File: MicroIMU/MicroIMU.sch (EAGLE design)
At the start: 18 parts, among them IC1 LSM303DLHC

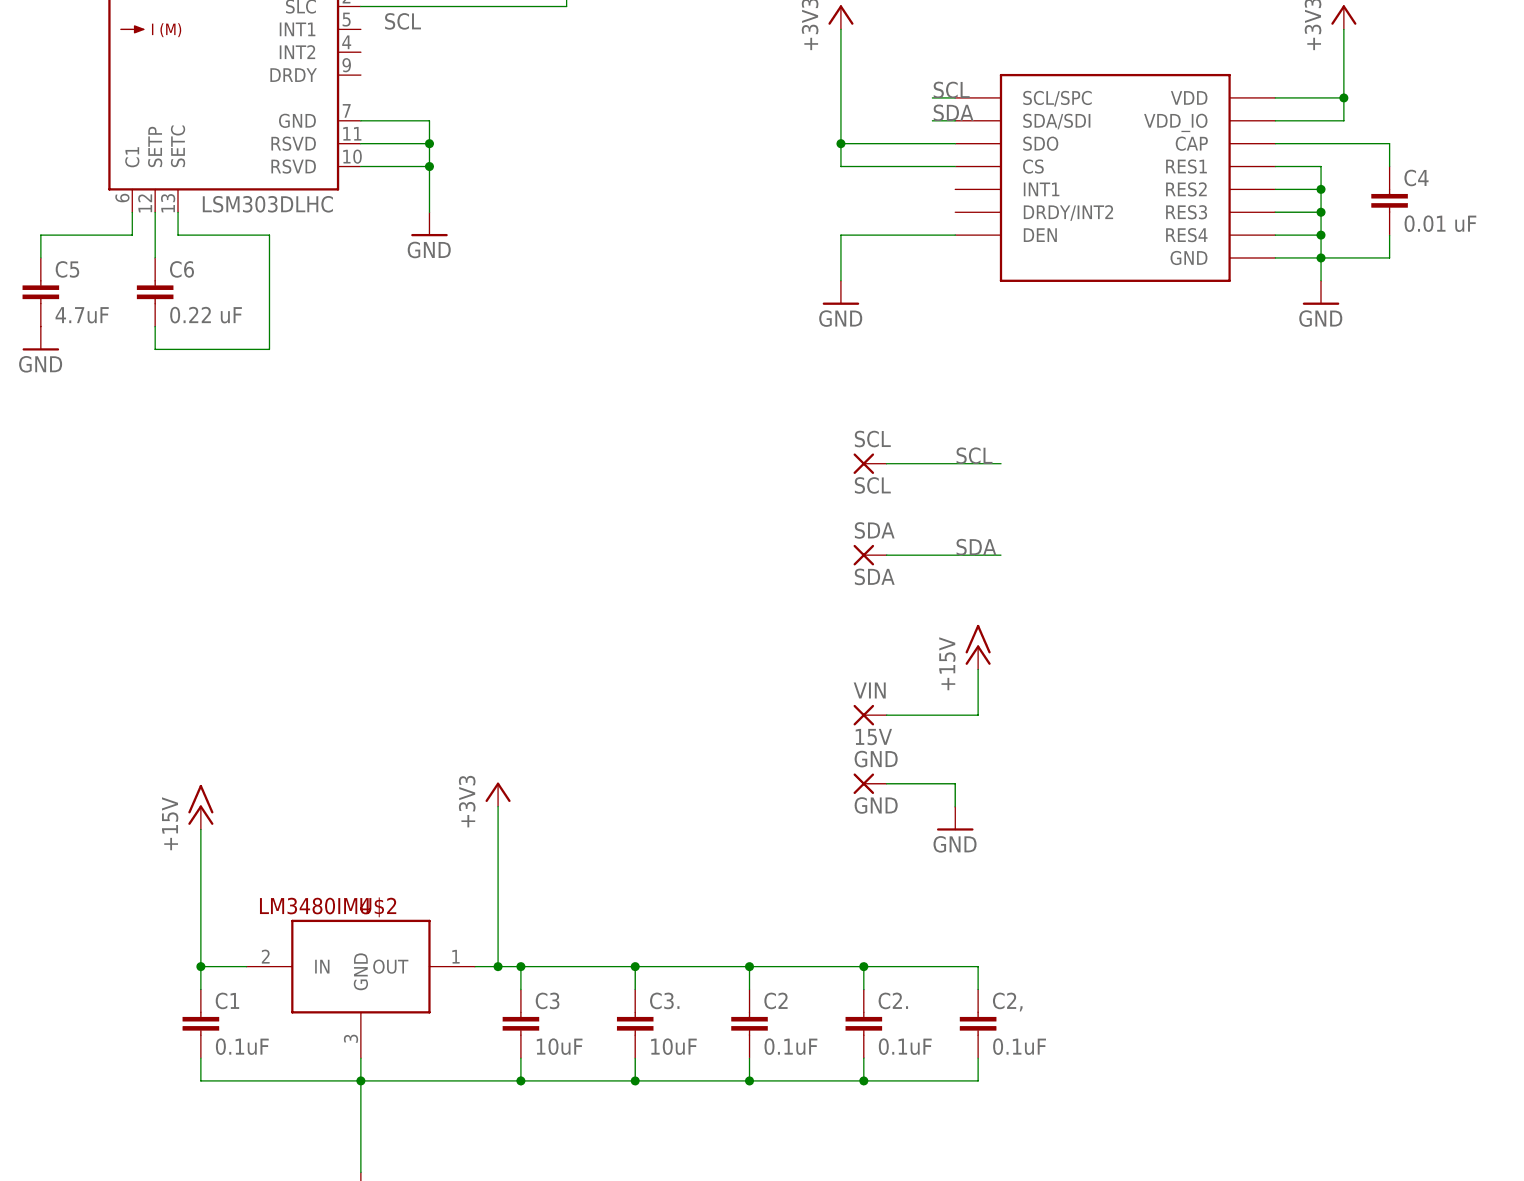
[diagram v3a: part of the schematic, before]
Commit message: Improved silkscreen labels
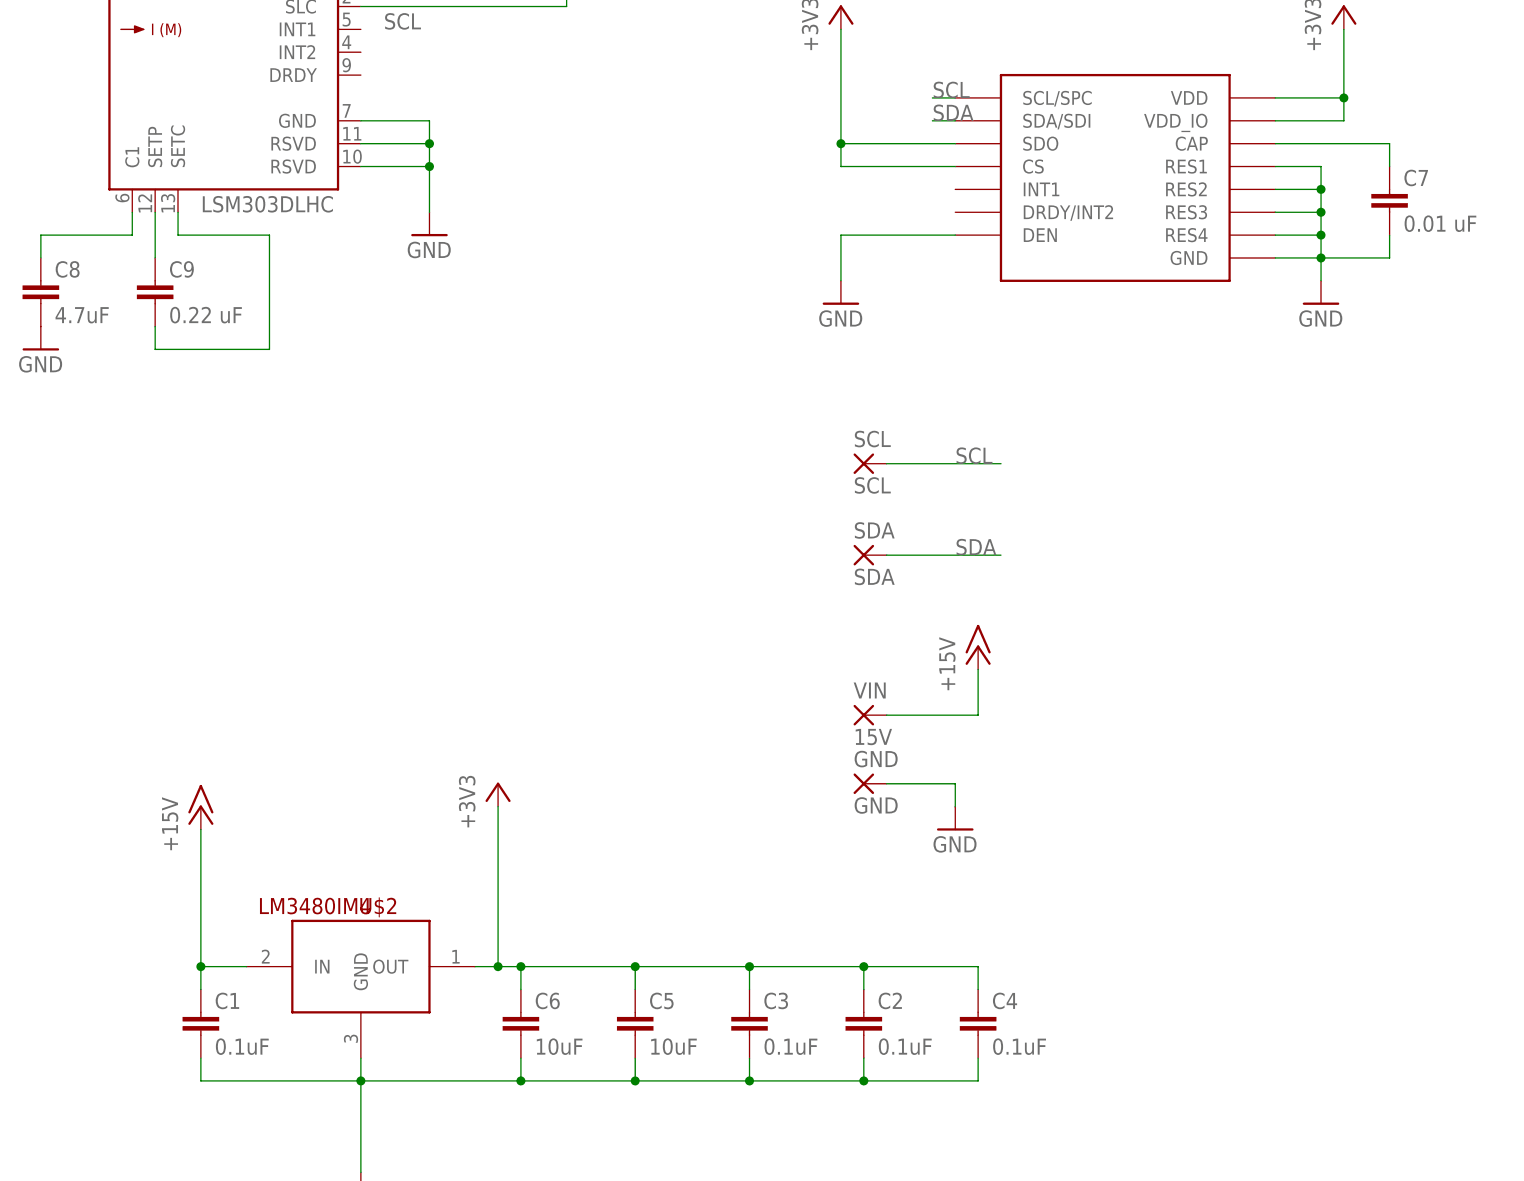
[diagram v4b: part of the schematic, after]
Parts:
- removed C2,, C2.: 0.1uF, resistor:C-EUC0201
- removed C3.: 10uF, resistor:C-EUC0603
- added C7: 0.01 uF, resistor:C-EUC0402
- added C8: 4.7uF, resistor:C-EUC0402
- added C9: 0.22 uF, resistor:C-EUC0201
- C3: value 10uF -> 0.1uF; device resistor:C-EUC0603 -> resistor:C-EUC0201
- C4: value 0.01 uF -> 0.1uF; device resistor:C-EUC0402 -> resistor:C-EUC0201
- C5: value 4.7uF -> 10uF; device resistor:C-EUC0402 -> resistor:C-EUC0603
- C6: value 0.22 uF -> 10uF; device resistor:C-EUC0201 -> resistor:C-EUC0603
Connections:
- net +3V3: now also C4.1, C5.1, C6.1; no longer C2,.1, C2..1, C3..1
- net GND: now also C6.2, C7.2, C8.2; no longer C2,.2, C2..2, C3..2
- net N$1: now also C8.1; no longer C5.1
- net N$2: now also C9.1; no longer C6.1
- net N$3: now also C9.2; no longer C6.2
- net N$9: now also C7.1; no longer C4.1
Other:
- moved on the sheet: C2, C3, C4, C5, C6
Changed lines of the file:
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@@
 <part name="R2" library="resistor" deviceset="R-US_" device="R0201" value="10k"/>
 <part name="+3V3" library="supply1" deviceset="+3V3" device=""/>
-<part name="C5" library="resistor" deviceset="C-EU" device="C0402" value="4.7uF"/>
+<part name="C8" library="resistor" deviceset="C-EU" device="C0402" value="4.7uF"/>
 <part name="GND4" library="supply1" deviceset="GND" device=""/>
-<part name="C6" library="resistor" deviceset="C-EU" device="C0201" value="0.22 uF"/>
+<part name="C9" library="resistor" deviceset="C-EU" device="C0201" value="0.22 uF"/>
 <part name="+3V4" library="supply1" deviceset="+3V3" device=""/>
 <part name="GND6" library="supply1" deviceset="GND" device=""/>
-<part name="C4" library="resistor" deviceset="C-EU" device="C0402" value="0.01 uF"/>
+<part name="C7" library="resistor" deviceset="C-EU" device="C0402" value="0.01 uF"/>
 <part name="GND" library="wirepad" deviceset="1,6/0,8" device="" value="GND"/>
 <part name="VIN" library="wirepad" deviceset="1,6/0,8" device="" value="15V"/>
@@
 <part name="SCL" library="wirepad" deviceset="1,6/0,8" device="" value="SCL"/>
 <part name="GND5" library="supply1" deviceset="GND" device=""/>
-<part name="C3" library="resistor" deviceset="C-EU" device="C0603" value="10uF"/>
-<part name="C3." library="resistor" deviceset="C-EU" device="C0603" value="10uF"/>
+<part name="C6" library="resistor" deviceset="C-EU" device="C0603" value="10uF"/>
+<part name="C5" library="resistor" deviceset="C-EU" device="C0603" value="10uF"/>
+<part name="C3" library="resistor" deviceset="C-EU" device="C0201" value="0.1uF"/>
 <part name="C2" library="resistor" deviceset="C-EU" device="C0201" value="0.1uF"/>
-<part name="C2." library="resistor" deviceset="C-EU" device="C0201" value="0.1uF"/>
 <part name="C1" library="resistor" deviceset="C-EU" device="C0201" value="0.1uF"/>
-<part name="C2," library="resistor" deviceset="C-EU" device="C0201" value="0.1uF"/>
+<part name="C4" library="resistor" deviceset="C-EU" device="C0201" value="0.1uF"/>
 </parts>
 <sheets>
@@
 <instance part="R2" gate="G$1" x="53.34" y="213.36" rot="R90"/>
 <instance part="+3V3" gate="G$1" x="35.56" y="231.14"/>
-<instance part="C5" gate="G$1" x="-5.08" y="175.26"/>
+<instance part="C8" gate="G$1" x="-5.08" y="175.26"/>
 <instance part="GND4" gate="1" x="-5.08" y="167.64"/>
-<instance part="C6" gate="G$1" x="7.62" y="175.26"/>
+<instance part="C9" gate="G$1" x="7.62" y="175.26"/>
 <instance part="+3V4" gate="G$1" x="83.82" y="205.74"/>
 <instance part="GND6" gate="1" x="83.82" y="172.72"/>
-<instance part="C4" gate="G$1" x="144.78" y="185.42"/>
+<instance part="C7" gate="G$1" x="144.78" y="185.42"/>
 <instance part="GND" gate="P" x="86.36" y="119.38"/>
 <instance part="VIN" gate="P" x="86.36" y="127"/>
@@
 <instance part="SCL" gate="P" x="86.36" y="154.94"/>
 <instance part="GND5" gate="1" x="96.52" y="114.3"/>
-<instance part="C3" gate="G$1" x="48.26" y="93.98"/>
-<instance part="C3." gate="G$1" x="60.96" y="93.98"/>
-<instance part="C2" gate="G$1" x="73.66" y="93.98"/>
-<instance part="C2." gate="G$1" x="86.36" y="93.98"/>
+<instance part="C6" gate="G$1" x="48.26" y="93.98"/>
+<instance part="C5" gate="G$1" x="60.96" y="93.98"/>
+<instance part="C3" gate="G$1" x="73.66" y="93.98"/>
+<instance part="C2" gate="G$1" x="86.36" y="93.98"/>
 <instance part="C1" gate="G$1" x="12.7" y="93.98"/>
-<instance part="C2," gate="G$1" x="99.06" y="93.98"/>
+<instance part="C4" gate="G$1" x="99.06" y="93.98"/>
 </instances>
 <busses>
@@
 <pinref part="GND2" gate="1" pin="GND"/>
 <wire x1="30.48" y1="88.9" x2="30.48" y2="86.36" width="0.1524" layer="91"/>
-<pinref part="C3" gate="G$1" pin="2"/>
+<pinref part="C6" gate="G$1" pin="2"/>
 <wire x1="30.48" y1="86.36" x2="30.48" y2="76.2" width="0.1524" layer="91"/>
 <wire x1="48.26" y1="88.9" x2="48.26" y2="86.36" width="0.1524" layer="91"/>
 <wire x1="48.26" y1="86.36" x2="30.48" y2="86.36" width="0.1524" layer="91"/>
 <junction x="30.48" y="86.36"/>
-<pinref part="C3." gate="G$1" pin="2"/>
+<pinref part="C5" gate="G$1" pin="2"/>
 <wire x1="60.96" y1="88.9" x2="60.96" y2="86.36" width="0.1524" layer="91"/>
 <wire x1="60.96" y1="86.36" x2="48.26" y2="86.36" width="0.1524" layer="91"/>
 <junction x="48.26" y="86.36"/>
-<pinref part="C2" gate="G$1" pin="2"/>
+<pinref part="C3" gate="G$1" pin="2"/>
 <wire x1="73.66" y1="88.9" x2="73.66" y2="86.36" width="0.1524" layer="91"/>
 <wire x1="73.66" y1="86.36" x2="60.96" y2="86.36" width="0.1524" layer="91"/>
 <junction x="60.96" y="86.36"/>
-<pinref part="C2." gate="G$1" pin="2"/>
+<pinref part="C2" gate="G$1" pin="2"/>
 <wire x1="86.36" y1="88.9" x2="86.36" y2="86.36" width="0.1524" layer="91"/>
 <wire x1="86.36" y1="86.36" x2="73.66" y2="86.36" width="0.1524" layer="91"/>
@@
 <wire x1="12.7" y1="88.9" x2="12.7" y2="86.36" width="0.1524" layer="91"/>
 <wire x1="12.7" y1="86.36" x2="30.48" y2="86.36" width="0.1524" layer="91"/>
-<pinref part="C2," gate="G$1" pin="2"/>
+<pinref part="C4" gate="G$1" pin="2"/>
 <wire x1="99.06" y1="88.9" x2="99.06" y2="86.36" width="0.1524" layer="91"/>
 <wire x1="99.06" y1="86.36" x2="86.36" y2="86.36" width="0.1524" layer="91"/>
@@
 <wire x1="137.16" y1="187.96" x2="137.16" y2="185.42" width="0.1524" layer="91"/>
 <junction x="137.16" y="185.42"/>
-<pinref part="C4" gate="G$1" pin="2"/>
+<pinref part="C7" gate="G$1" pin="2"/>
 <wire x1="144.78" y1="180.34" x2="144.78" y2="177.8" width="0.1524" layer="91"/>
 <wire x1="144.78" y1="177.8" x2="137.16" y2="177.8" width="0.1524" layer="91"/>
@@
 </segment>
 <segment>
-<pinref part="C5" gate="G$1" pin="2"/>
+<pinref part="C8" gate="G$1" pin="2"/>
 <pinref part="GND4" gate="1" pin="GND"/>
 </segment>
@@
 <pinref part="U$2" gate="G$1" pin="OUT"/>
 <wire x1="43.18" y1="99.06" x2="45.72" y2="99.06" width="0.1524" layer="91"/>
-<pinref part="C3" gate="G$1" pin="1"/>
+<pinref part="C6" gate="G$1" pin="1"/>
 <wire x1="48.26" y1="96.52" x2="48.26" y2="99.06" width="0.1524" layer="91"/>
 <wire x1="48.26" y1="99.06" x2="45.72" y2="99.06" width="0.1524" layer="91"/>
 <junction x="45.72" y="99.06"/>
-<pinref part="C3." gate="G$1" pin="1"/>
+<pinref part="C5" gate="G$1" pin="1"/>
 <wire x1="60.96" y1="96.52" x2="60.96" y2="99.06" width="0.1524" layer="91"/>
 <wire x1="60.96" y1="99.06" x2="48.26" y2="99.06" width="0.1524" layer="91"/>
 <junction x="48.26" y="99.06"/>
-<pinref part="C2" gate="G$1" pin="1"/>
+<pinref part="C3" gate="G$1" pin="1"/>
 <wire x1="73.66" y1="96.52" x2="73.66" y2="99.06" width="0.1524" layer="91"/>
 <wire x1="73.66" y1="99.06" x2="60.96" y2="99.06" width="0.1524" layer="91"/>
 <junction x="60.96" y="99.06"/>
-<pinref part="C2." gate="G$1" pin="1"/>
+<pinref part="C2" gate="G$1" pin="1"/>
 <wire x1="86.36" y1="96.52" x2="86.36" y2="99.06" width="0.1524" layer="91"/>
 <wire x1="86.36" y1="99.06" x2="73.66" y2="99.06" width="0.1524" layer="91"/>
@@
 <wire x1="86.36" y1="99.06" x2="99.06" y2="99.06" width="0.1524" layer="91"/>
 <junction x="86.36" y="99.06"/>
-<pinref part="C2," gate="G$1" pin="1"/>
+<pinref part="C4" gate="G$1" pin="1"/>
 <wire x1="99.06" y1="99.06" x2="99.06" y2="96.52" width="0.1524" layer="91"/>
 </segment>
@@
 <segment>
 <pinref part="IC1" gate="G$1" pin="SETP"/>
-<pinref part="C6" gate="G$1" pin="1"/>
+<pinref part="C9" gate="G$1" pin="1"/>
 <wire x1="7.62" y1="182.88" x2="7.62" y2="177.8" width="0.1524" layer="91"/>
 </segment>
@@
 <wire x1="20.32" y1="180.34" x2="20.32" y2="167.64" width="0.1524" layer="91"/>
 <wire x1="20.32" y1="167.64" x2="7.62" y2="167.64" width="0.1524" layer="91"/>
-<pinref part="C6" gate="G$1" pin="2"/>
+<pinref part="C9" gate="G$1" pin="2"/>
 <wire x1="7.62" y1="167.64" x2="7.62" y2="170.18" width="0.1524" layer="91"/>
 </segment>
@@
 <wire x1="5.08" y1="182.88" x2="5.08" y2="180.34" width="0.1524" layer="91"/>
 <wire x1="5.08" y1="180.34" x2="-5.08" y2="180.34" width="0.1524" layer="91"/>
-<pinref part="C5" gate="G$1" pin="1"/>
+<pinref part="C8" gate="G$1" pin="1"/>
 <wire x1="-5.08" y1="180.34" x2="-5.08" y2="177.8" width="0.1524" layer="91"/>
 </segment>
@@
 <pinref part="U$1" gate="G$1" pin="CAP"/>
 <wire x1="132.08" y1="190.5" x2="144.78" y2="190.5" width="0.1524" layer="91"/>
-<pinref part="C4" gate="G$1" pin="1"/>
+<pinref part="C7" gate="G$1" pin="1"/>
 <wire x1="144.78" y1="190.5" x2="144.78" y2="187.96" width="0.1524" layer="91"/>
 </segment>
